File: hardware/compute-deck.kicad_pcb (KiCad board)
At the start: 4 copper layers, 70.5 x 88.9 mm, 64 parts, among them J1 USB_C_Receptacle_USB2.0_16P, J2 Conn_01x02, J3 Conn_01x02, J4 Conn_01x08, Q1 BSS138, Q2 Q_PMOS, SW1 SW_Push, SW2 SW_SPDT, U1 IP5306, U2 RP2040, U3 W25Q128JVS, U4 BBQ10KBD, Y1 12MHz

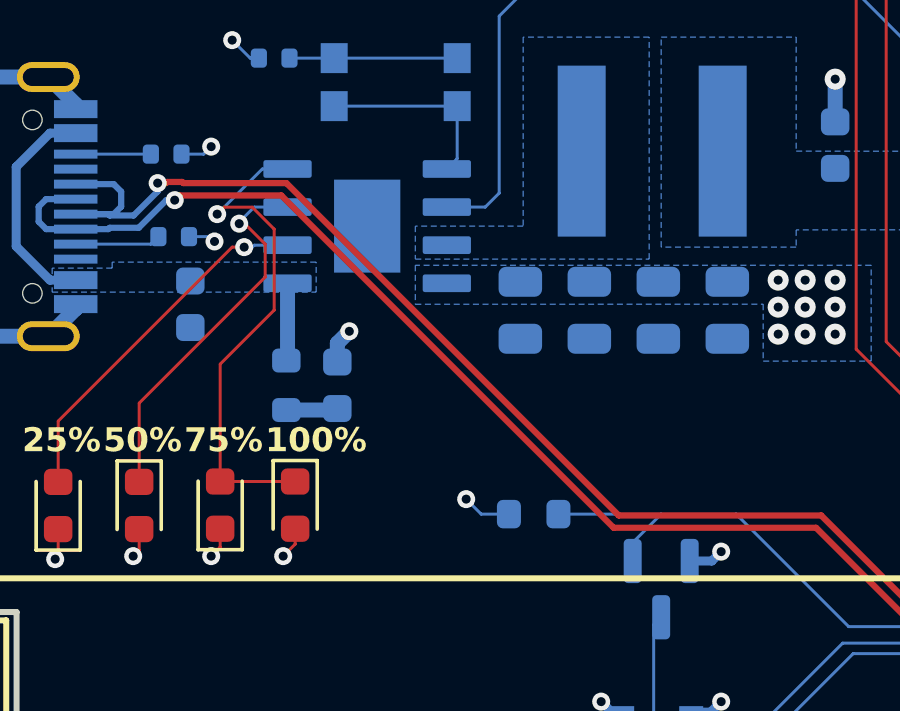
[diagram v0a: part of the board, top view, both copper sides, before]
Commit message: start revision to on-board SoC
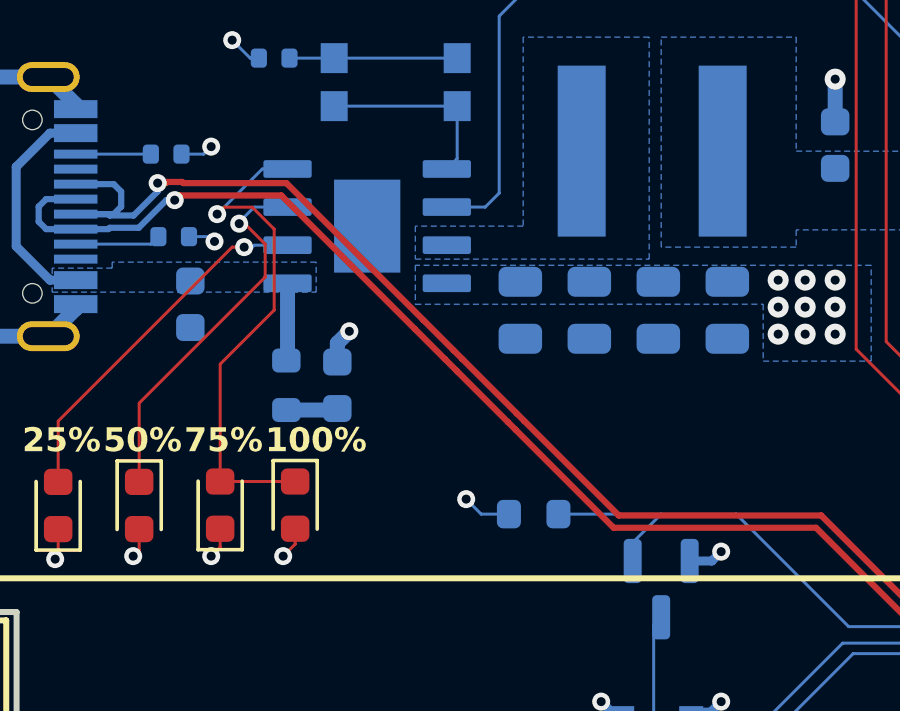
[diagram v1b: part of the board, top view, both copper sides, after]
